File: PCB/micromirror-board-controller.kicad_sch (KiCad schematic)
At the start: 18 parts, among them J1 RPi header, J2 DMD board PWR, J3 Conn_01x03_Female, J4 51-pin conn, J5 Barrel_Jack, J6 Extra GPIO, J7 5V Ext, J8 STEMMA, U2 CUI P78E05-1000

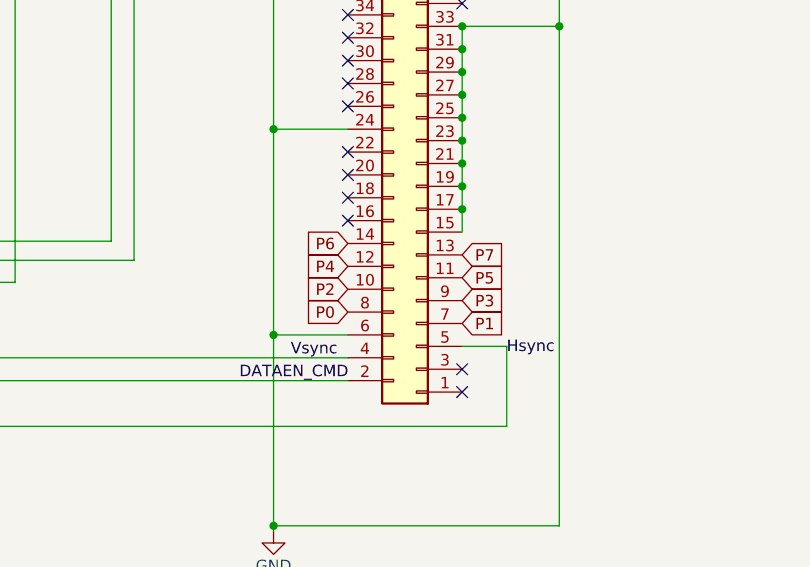
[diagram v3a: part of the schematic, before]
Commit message: Fix incorrect pinout for pixeldata
Corrected the incorrect pinout of the pixeldata section of the FPC connector. Even and odd pins had to be switched (P0 <-> P1) etc. Fixes https://github.com/openMLA/photon-ultra-controller/issues/2.
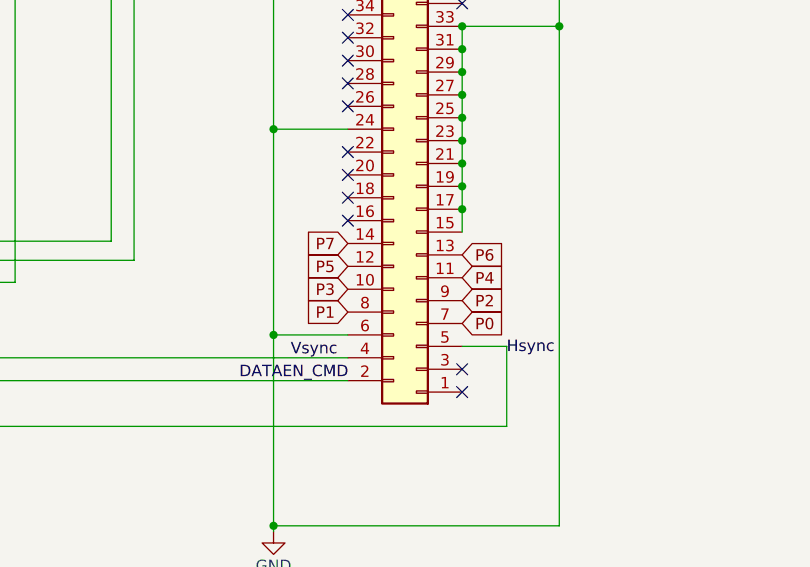
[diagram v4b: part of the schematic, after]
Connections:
- net P0: now also J4.7 (P1); no longer J4.8 (P0)
- net P1: now also J4.8 (P0); no longer J4.7 (P1)
- net P2: now also J4.9 (P3); no longer J4.10 (P2)
- net P3: now also J4.10 (P2); no longer J4.9 (P3)
- net P4: now also J4.11 (P5); no longer J4.12 (P4)
- net P5: now also J4.12 (P4); no longer J4.11 (P5)
- net P6: now also J4.13 (P7); no longer J4.14 (P6)
- net P7: now also J4.14 (P6); no longer J4.13 (P7)
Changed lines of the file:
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@@
     )
   )
-  (global_label "P1" (shape input) (at 202.565 135.89 0) (fields_autoplaced)
-    (effects (font (size 1.27 1.27)) (justify left))
-    (property "Intersheetrefs" "${INTERSHEET_REFS}" (at 207.9503 135.89 0)
-      (effects (font (size 1.27 1.27)) (justify left) hide)
+  (global_label "P1" (shape input) (at 189.865 134.62 180) (fields_autoplaced)
+    (effects (font (size 1.27 1.27)) (justify right))
+    (property "Intersheetrefs" "${INTERSHEET_REFS}" (at 184.4797 134.62 0)
+      (effects (font (size 1.27 1.27)) (justify right) hide)
     )
   )
@@
     )
   )
-  (global_label "P4" (shape input) (at 189.865 129.54 180) (fields_autoplaced)
-    (effects (font (size 1.27 1.27)) (justify right))
-    (property "Intersheetrefs" "${INTERSHEET_REFS}" (at 184.4797 129.54 0)
-      (effects (font (size 1.27 1.27)) (justify right) hide)
+  (global_label "P4" (shape input) (at 202.565 130.81 0) (fields_autoplaced)
+    (effects (font (size 1.27 1.27)) (justify left))
+    (property "Intersheetrefs" "${INTERSHEET_REFS}" (at 207.9503 130.81 0)
+      (effects (font (size 1.27 1.27)) (justify left) hide)
     )
   )
@@
     )
   )
-  (global_label "P7" (shape input) (at 202.565 128.27 0) (fields_autoplaced)
-    (effects (font (size 1.27 1.27)) (justify left))
-    (property "Intersheetrefs" "${INTERSHEET_REFS}" (at 207.9503 128.27 0)
-      (effects (font (size 1.27 1.27)) (justify left) hide)
+  (global_label "P7" (shape input) (at 189.865 127 180) (fields_autoplaced)
+    (effects (font (size 1.27 1.27)) (justify right))
+    (property "Intersheetrefs" "${INTERSHEET_REFS}" (at 184.4797 127 0)
+      (effects (font (size 1.27 1.27)) (justify right) hide)
     )
   )
@@
     )
   )
-  (global_label "P3" (shape input) (at 202.565 133.35 0) (fields_autoplaced)
-    (effects (font (size 1.27 1.27)) (justify left))
-    (property "Intersheetrefs" "${INTERSHEET_REFS}" (at 207.9503 133.35 0)
-      (effects (font (size 1.27 1.27)) (justify left) hide)
+  (global_label "P3" (shape input) (at 189.865 132.08 180) (fields_autoplaced)
+    (effects (font (size 1.27 1.27)) (justify right))
+    (property "Intersheetrefs" "${INTERSHEET_REFS}" (at 184.4797 132.08 0)
+      (effects (font (size 1.27 1.27)) (justify right) hide)
     )
   )
-  (global_label "P5" (shape input) (at 202.565 130.81 0) (fields_autoplaced)
-    (effects (font (size 1.27 1.27)) (justify left))
-    (property "Intersheetrefs" "${INTERSHEET_REFS}" (at 207.9503 130.81 0)
-      (effects (font (size 1.27 1.27)) (justify left) hide)
+  (global_label "P5" (shape input) (at 189.865 129.54 180) (fields_autoplaced)
+    (effects (font (size 1.27 1.27)) (justify right))
+    (property "Intersheetrefs" "${INTERSHEET_REFS}" (at 184.4797 129.54 0)
+      (effects (font (size 1.27 1.27)) (justify right) hide)
     )
   )
@@
     )
   )
-  (global_label "P6" (shape input) (at 189.865 127 180) (fields_autoplaced)
-    (effects (font (size 1.27 1.27)) (justify right))
-    (property "Intersheetrefs" "${INTERSHEET_REFS}" (at 184.4797 127 0)
-      (effects (font (size 1.27 1.27)) (justify right) hide)
+  (global_label "P6" (shape input) (at 202.565 128.27 0) (fields_autoplaced)
+    (effects (font (size 1.27 1.27)) (justify left))
+    (property "Intersheetrefs" "${INTERSHEET_REFS}" (at 207.9503 128.27 0)
+      (effects (font (size 1.27 1.27)) (justify left) hide)
     )
   )
@@
     )
   )
-  (global_label "P0" (shape input) (at 189.865 134.62 180) (fields_autoplaced)
-    (effects (font (size 1.27 1.27)) (justify right))
-    (property "Intersheetrefs" "${INTERSHEET_REFS}" (at 184.4797 134.62 0)
-      (effects (font (size 1.27 1.27)) (justify right) hide)
+  (global_label "P0" (shape input) (at 202.565 135.89 0) (fields_autoplaced)
+    (effects (font (size 1.27 1.27)) (justify left))
+    (property "Intersheetrefs" "${INTERSHEET_REFS}" (at 207.9503 135.89 0)
+      (effects (font (size 1.27 1.27)) (justify left) hide)
     )
   )
@@
     )
   )
-  (global_label "P2" (shape input) (at 189.865 132.08 180) (fields_autoplaced)
-    (effects (font (size 1.27 1.27)) (justify right))
-    (property "Intersheetrefs" "${INTERSHEET_REFS}" (at 184.4797 132.08 0)
-      (effects (font (size 1.27 1.27)) (justify right) hide)
+  (global_label "P2" (shape input) (at 202.565 133.35 0) (fields_autoplaced)
+    (effects (font (size 1.27 1.27)) (justify left))
+    (property "Intersheetrefs" "${INTERSHEET_REFS}" (at 207.9503 133.35 0)
+      (effects (font (size 1.27 1.27)) (justify left) hide)
     )
   )
